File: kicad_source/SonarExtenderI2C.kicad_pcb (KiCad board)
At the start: 2 copper layers, 100 x 60 mm, 48 parts, among them CN2 CONN_01X04, CN3 CONN_01X04, CN4 CONN_01X04, CN5 CONN_01X04, CN6 CONN_01X04, P1 CONN_01X06, U1 NE555-IC_logic, U10 74xx590-IC_logic, U11 74xx590-IC_logic, U12 74xx590-IC_logic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

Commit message: finished pcb layout
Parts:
- removed U19: 74xx32, SOIC:SOIC-14_3.9x8.7mm_Pitch1.27mm
- added C18: C_0603, capacitors:C_0603, F.Cu at (135.4, 56.9)
- added C19: C_0603, capacitors:C_0603, F.Cu at (129.6, 45.0)
- added C2: C_0603, capacitors:C_0603, F.Cu at (142.9, 77.3)
- added C20: C_0603, capacitors:C_0603, F.Cu at (135.1, 44.5)
- added C21: C_0603, capacitors:C_0603, F.Cu at (168.7, 42.2)
- added C22: C_0603, capacitors:C_0603, F.Cu at (153.9, 53.3)
- added L1: Label, labels:jecc_logo_7.2x2.2, F.Cu at (118.0, 45.2)
- added L2: Label, labels:Top, F.Cu at (185.8, 49.6)
- added L3: Label, labels:Bot, F.Cu at (185.6, 49.6)
- added L4: Label, labels:generationmake_logo, F.Cu at (106.0, 61.2)
- added R5: 10k, resistors:R_0603, F.Cu at (180.0, 64.5)
- added R6: 10k, resistors:R_0603, F.Cu at (182.0, 65.5)
- added U3: 74xx08, SOIC:SOIC-14_3.9x8.7mm_Pitch1.27mm, F.Cu at (166.6, 47.8)
- U18: value 74xx08 -> 74xx32
- moved R1 153.5 mm to (96.3, 82.0), turned to 90 degrees
- moved R2 149.6 mm to (101.1, 84.3)
- moved C11 136.0 mm to (113.5, 70.9), turned to 90 degrees
- moved U1 135.7 mm to (101.1, 80.5), turned to 180 degrees
- moved U5 117.0 mm to (127.8, 80.0)
- moved R3 114.1 mm to (101.9, 48.8), turned to 90 degrees
- moved C16 112.2 mm to (104.6, 43.7)
- moved C17 112.1 mm to (108.7, 43.7), turned to 180 degrees
- moved R4 110.6 mm to (106.7, 51.3)
- moved C4 110.5 mm to (98.8, 76.7)
- moved C5 109.9 mm to (103.4, 76.7), turned to 180 degrees
- moved C12 107.2 mm to (127.3, 70.9), turned to 90 degrees
- moved U14 104.7 mm to (106.7, 47.5), turned to 180 degrees
- moved C15 100.2 mm to (111.5, 49.0), turned to 270 degrees
- moved U16 95.7 mm to (127.3, 50.5)
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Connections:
- U1 pad 4: GND -> +3V3
- U13 pad 1: Net-(U13-Pad1) -> /STATUS_ECHO
- U13 pad 10: Net-(U13-Pad10) -> GND
- U13 pad 11: Net-(U13-Pad11) -> GND
- U13 pad 12: Net-(U13-Pad12) -> GND
- U13 pad 13: /STATUS_ECHO -> Net-(U13-Pad13)
- U13 pad 14: Net-(U13-Pad14) -> +3V3
- U13 pad 2: Net-(U13-Pad2) -> /ECHO0
- U13 pad 3: /ECHO0 -> /ECHO1
- U13 pad 4: /ECHO1 -> /ECHO2
- U13 pad 5: /ECHO2 -> /ECHO3
- U13 pad 7: Net-(U13-Pad7) -> GND
- U13 pad 9: Net-(U13-Pad9) -> GND
- U14 pad 4: GND -> +3V3
- U15 pad 5: GND -> /auto/E3
- U15 pad 7: Net-(U15-Pad7) -> I2C_INT
- U16 pad 12: /auto/E3# -> Net-(U15-Pad6)
- U18 pad 1: ENABLE0 -> /auto/E0
- U18 pad 10: ENABLE2 -> /auto/E2
- U18 pad 11: CNT3 -> EN3
- U18 pad 12: /auto/E3# -> T3
- U18 pad 13: ENABLE3 -> /auto/E3
- U18 pad 2: /auto/E0# -> T0
- U18 pad 3: CNT0 -> EN0
- U18 pad 4: ENABLE1 -> /auto/E1
- U18 pad 5: /auto/E1# -> T1
- U18 pad 6: CNT1 -> EN1
- U18 pad 8: CNT2 -> EN2
- U18 pad 9: /auto/E2# -> T2
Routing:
- net +3V3: track 0.00 -> 339.4 mm, vias 0 -> 18
- net /CLK_10KHZ: track 0.00 -> 98.7 mm, vias 0 -> 2
- net +5V: track 0.00 -> 97.5 mm
- net CNT0: track 0.00 -> 97.0 mm, vias 0 -> 2
- net /D7: track 0.00 -> 89.4 mm, vias 0 -> 5
- net /D6: track 0.00 -> 84.9 mm, vias 0 -> 5
- net /D1: track 0.00 -> 83.1 mm, vias 0 -> 5
- net /D2: track 0.00 -> 81.0 mm, vias 0 -> 5
- net AUTO: track 0.00 -> 80.7 mm, vias 0 -> 1
- net /D5: track 0.00 -> 80.5 mm, vias 0 -> 5
- net CNT1: track 0.00 -> 80.4 mm, vias 0 -> 2
- net /D3: track 0.00 -> 79.2 mm, vias 0 -> 5
- net /D4: track 0.00 -> 77.7 mm, vias 0 -> 5
- net /D0: track 0.00 -> 75.1 mm, vias 0 -> 5
- net /TRIG0: track 0.00 -> 71.8 mm, vias 0 -> 2
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- added copper zone on B.Cu, net GND
- added copper zone on F.Cu, net GND

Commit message: reacted to review
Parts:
- added C23: 47uF 16V, capacitors:c_elec_6.3x4.5, F.Cu at (161.9, 67.2)
- added C24: 47uF 16V, capacitors:c_elec_6.3x4.5, F.Cu at (178.7, 93.0)
- added D1: Led_Small, LEDs:LED_0603, F.Cu at (95.2, 74.5)
- added D2: Led_Small, LEDs:LED_0603, F.Cu at (114.4, 92.1)
- added D3: Led_Small, LEDs:LED_0603, F.Cu at (113.6, 73.2)
- added D4: Led_Small, LEDs:LED_0603, F.Cu at (126.6, 73.2)
- added D5: Led_Small, LEDs:LED_0603, F.Cu at (140.6, 73.2)
- added D6: Led_Small, LEDs:LED_0603, F.Cu at (155.0, 73.2)
- added R10: 220, resistors:R_0603, F.Cu at (123.8, 73.2)
- added R11: 220, resistors:R_0603, F.Cu at (137.8, 73.2)
- added R12: 220, resistors:R_0603, F.Cu at (152.2, 73.2)
- added R7: 220, resistors:R_0603, F.Cu at (95.2, 77.3)
- added R8: 320, resistors:R_0603, F.Cu at (113.6, 89.5)
- added R9: 220, resistors:R_0603, F.Cu at (110.8, 73.2)
- C1: value C_0603 -> 1nF
- C10, C11, C12, C13, C14, C18, C19, C2, C20, C21, C22, C3, C5, C6, C7, C8, C9: value C_0603 -> 100nF
- C15: value 100nF -> 1uF
- C16: value 100nF -> 10nF
- C4: value C_0603 -> 10nF
- R1, R3: value R_0603 -> 120k
- R2, R4: value R_0603 -> 12k
- moved L4 2.65 mm to (108.5, 62.2)
- moved L2 0.10 mm to (185.7, 49.6)
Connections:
- U1 pad 1: (no net) -> GND
- U14 pad 1: (no net) -> GND
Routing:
- net GND: track 18.4 -> 49.1 mm, vias 57 -> 62
- net +3V3: track 339.4 -> 347.9 mm, vias 18 -> 19
- net +5V: track 97.5 -> 102.9 mm, vias 0 -> 1
- net CNT0: track 97.0 -> 99.6 mm
- net CNT1: track 80.4 -> 82.4 mm
- net CNT2: track 65.1 -> 67.0 mm
- net CNT3: track 56.3 -> 58.2 mm
- net Net-(D2-Pad2): track 0.00 -> 1.83 mm
- net Net-(D1-Pad2): track 0.00 -> 1.36 mm
- net Net-(D6-Pad2): track 0.00 -> 1.30 mm
- net Net-(D4-Pad2): track 0.00 -> 1.30 mm
- net Net-(D3-Pad2): track 0.00 -> 1.30 mm
- net Net-(D5-Pad2): track 0.00 -> 1.30 mm
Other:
- board text added: "POWER 3V3"
- board text added: "POWER 5V"
- board text added: "SENSOR 0"
- board text added: "SENSOR 1"
- board text added: "SENSOR 2"
- board text added: "SENSOR 3"
- board text added: "SonarExtenderI2C"

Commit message: updated logic table
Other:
- board text added: "v0.1"
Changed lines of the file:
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@@
   (general
     (thickness 1.6)
-    (drawings 15)
+    (drawings 16)
     (tracks 1416)
     (zones 0)
@@
     )
   )
+  (gr_text v0.1 (at 95.1 89.2) (layer F.SilkS)
+    (effects (font (size 1.5 1.5) (thickness 0.3)))
+  )
   (gr_text SonarExtenderI2C (at 93.20784 58.42508 90) (layer F.Cu)

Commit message: added pause mode for automate
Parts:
- D1, D2, D3, D4, D5, D6: value Led_Small -> 150060GS75000
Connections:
- R10 pad 1: CNT1 -> ENABLE1
- R11 pad 1: CNT2 -> ENABLE2
- R12 pad 1: CNT3 -> ENABLE3
- R9 pad 1: CNT0 -> ENABLE0
- U10 pad 14: CNT1 -> ENABLE1
- U10 pad 9: Net-(U10-Pad9) -> (no net)
- U11 pad 14: CNT2 -> ENABLE2
- U11 pad 9: Net-(U11-Pad9) -> (no net)
- U12 pad 14: CNT3 -> ENABLE3
- U12 pad 9: Net-(U12-Pad9) -> (no net)
- U13 pad 13: Net-(U13-Pad13) -> (no net)
- U13 pad 6: Net-(U13-Pad6) -> (no net)
- U13 pad 8: Net-(U13-Pad8) -> (no net)
- U14 pad 3: /auto/CLK_10Hz -> Net-(U14-Pad3)
- U15 pad 10: Net-(U15-Pad10) -> (no net)
- U15 pad 11: Net-(U15-Pad11) -> (no net)
- U15 pad 14: Net-(U15-Pad14) -> (no net)
- U15 pad 15: Net-(U15-Pad15) -> (no net)
- U15 pad 2: Net-(U15-Pad2) -> (no net)
- U15 pad 4: AUTO -> /auto/AUTOEN
- U16 pad 1: AUTO -> /auto/AUTOEN
- U16 pad 2: AUTO -> /auto/AUTOEN
- U17 pad 11: /auto/E2# -> (no net)
- U17 pad 14: /auto/E3# -> (no net)
- U17 pad 3: /auto/E0# -> (no net)
- U17 pad 6: /auto/E1# -> (no net)
- U2 pad 1: Net-(U2-Pad1) -> (no net)
- U3 pad 1: ENABLE0 -> Net-(U14-Pad3)
- U3 pad 10: ENABLE2 -> (no net)
- U3 pad 11: CNT3 -> (no net)
- U3 pad 12: /auto/E3# -> (no net)
- U3 pad 13: ENABLE3 -> (no net)
- U3 pad 2: /auto/E0# -> PAUSE
- U3 pad 3: CNT0 -> /auto/CLK_10Hz
- U3 pad 4: ENABLE1 -> AUTO
- U3 pad 5: /auto/E1# -> PAUSE
- U3 pad 6: CNT1 -> /auto/AUTOEN
- U3 pad 8: CNT2 -> (no net)
- U3 pad 9: /auto/E2# -> (no net)
- U4 pad 10: Net-(U4-Pad10) -> PAUSE
- U4 pad 7: Net-(U4-Pad7) -> (no net)
- U4 pad 9: Net-(U4-Pad9) -> (no net)
- U6 pad 10: Net-(U6-Pad10) -> (no net)
- U6 pad 15: Net-(U6-Pad15) -> (no net)
- U6 pad 2: Net-(U6-Pad2) -> (no net)
- U6 pad 7: Net-(U6-Pad7) -> (no net)
- U7 pad 10: Net-(U7-Pad10) -> (no net)
- U7 pad 12: Net-(U7-Pad12) -> (no net)
- U9 pad 14: CNT0 -> ENABLE0
- U9 pad 9: Net-(U9-Pad9) -> (no net)
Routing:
- net CNT0: track 99.6 -> 0.00 mm, vias 2 -> 0
- net CNT1: track 82.4 -> 0.00 mm, vias 2 -> 0
- net ENABLE0: track 16.6 -> 96.8 mm, vias 2 -> 0
- net ENABLE1: track 11.0 -> 86.0 mm
- net AUTO: track 80.7 -> 11.4 mm, vias 1 -> 0
- net CNT2: track 67.0 -> 0.00 mm, vias 2 -> 0
- net ENABLE2: track 5.45 -> 71.7 mm, vias 0 -> 2
- net /auto/AUTOEN: track 0.00 -> 65.9 mm, vias 0 -> 1
- net Net-(U14-Pad3): track 0.00 -> 58.8 mm
- net CNT3: track 58.2 -> 0.00 mm, vias 2 -> 0
- net ENABLE3: track 5.56 -> 60.0 mm, vias 0 -> 2
- net /auto/E3#: track 35.6 -> 0.00 mm
- net /auto/E2#: track 34.1 -> 0.00 mm, vias 2 -> 0
- net /auto/E0#: track 31.0 -> 0.00 mm
- net /auto/CLK_10Hz: track 61.8 -> 31.3 mm
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
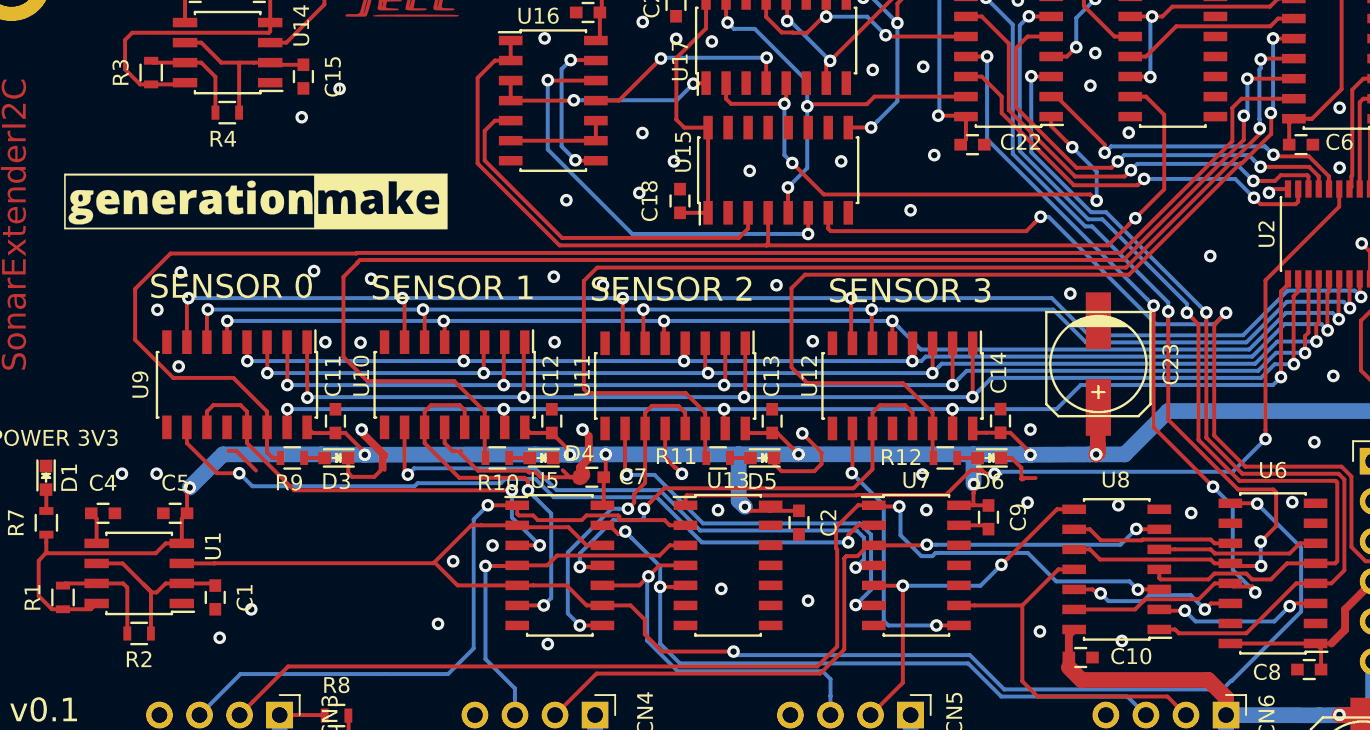
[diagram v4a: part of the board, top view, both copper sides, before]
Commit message: layout changed
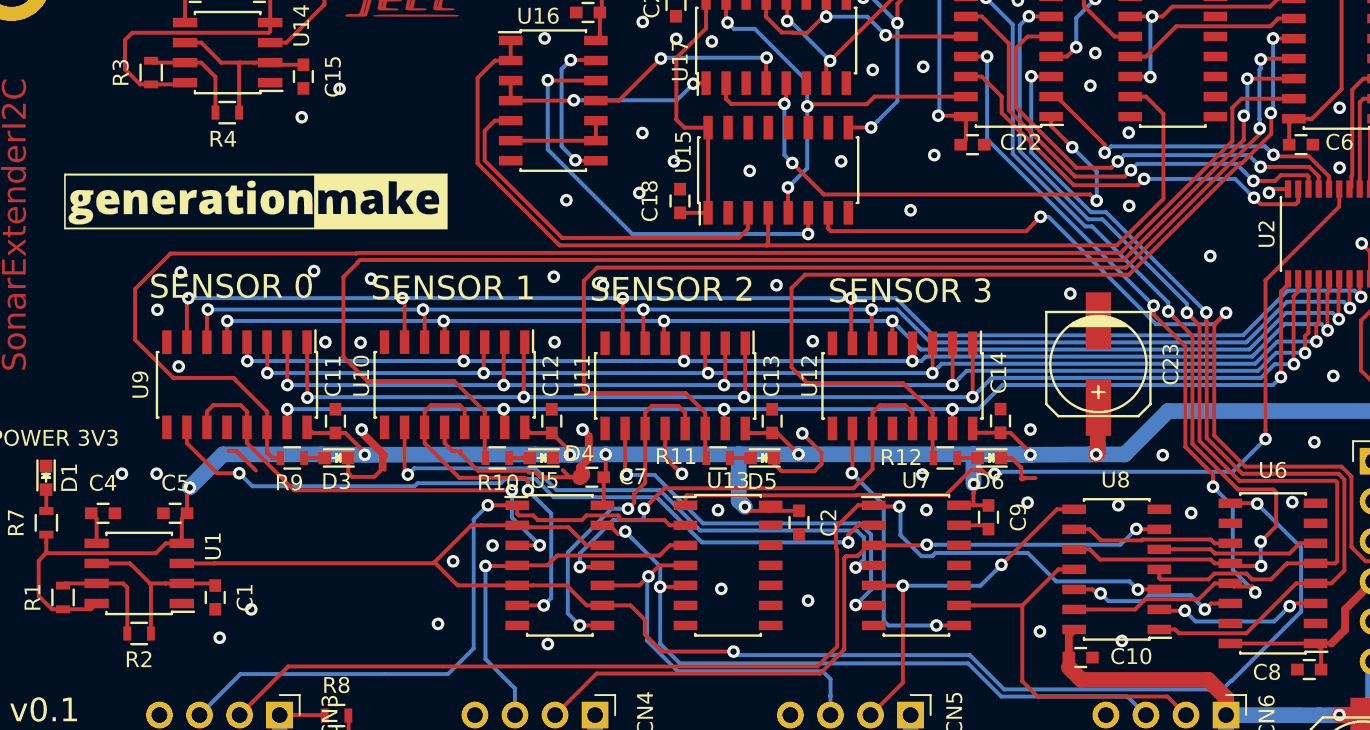
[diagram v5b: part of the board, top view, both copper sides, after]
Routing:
- net Net-(C1-Pad1): track 11.9 -> 11.3 mm
- net /auto/AUTOEN: track 65.9 -> 66.1 mm, vias 1 -> 0
- net GND: vias 68 -> 70

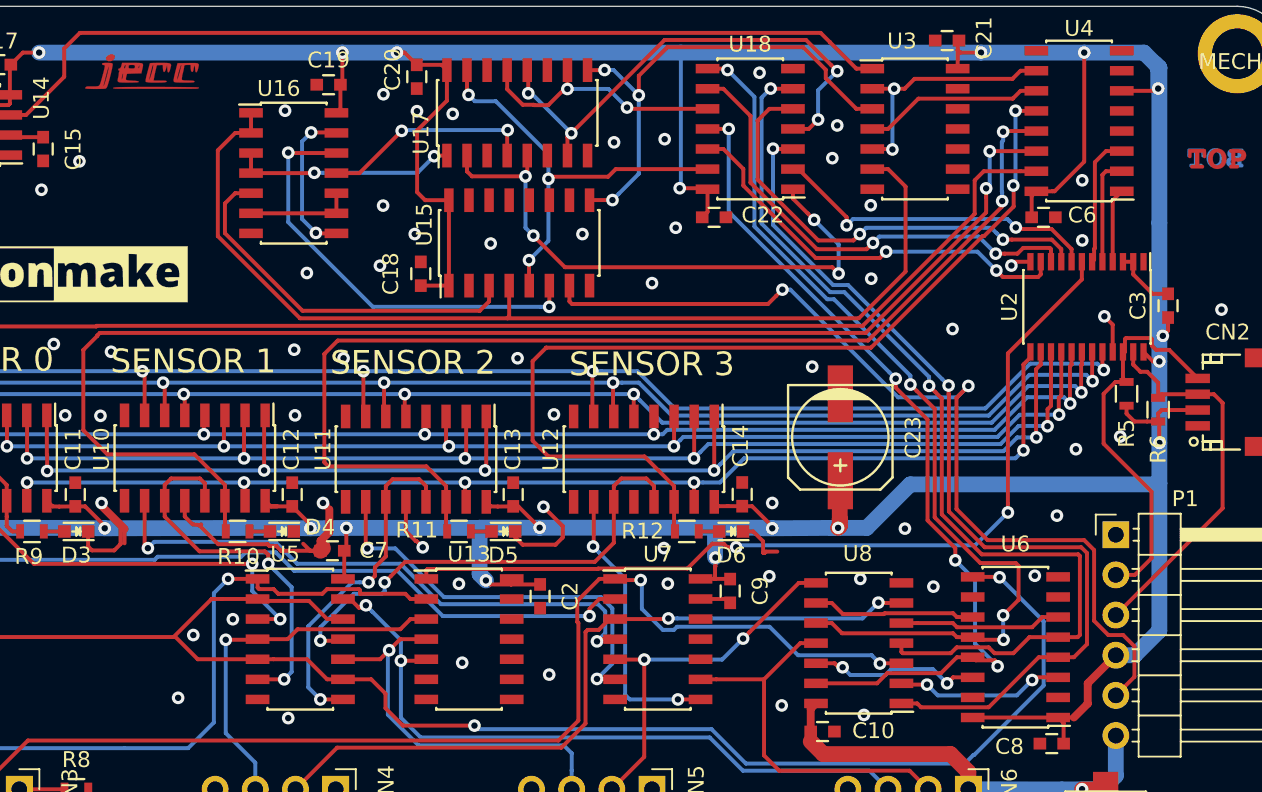
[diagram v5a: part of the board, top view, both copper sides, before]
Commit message: added EN LEDS
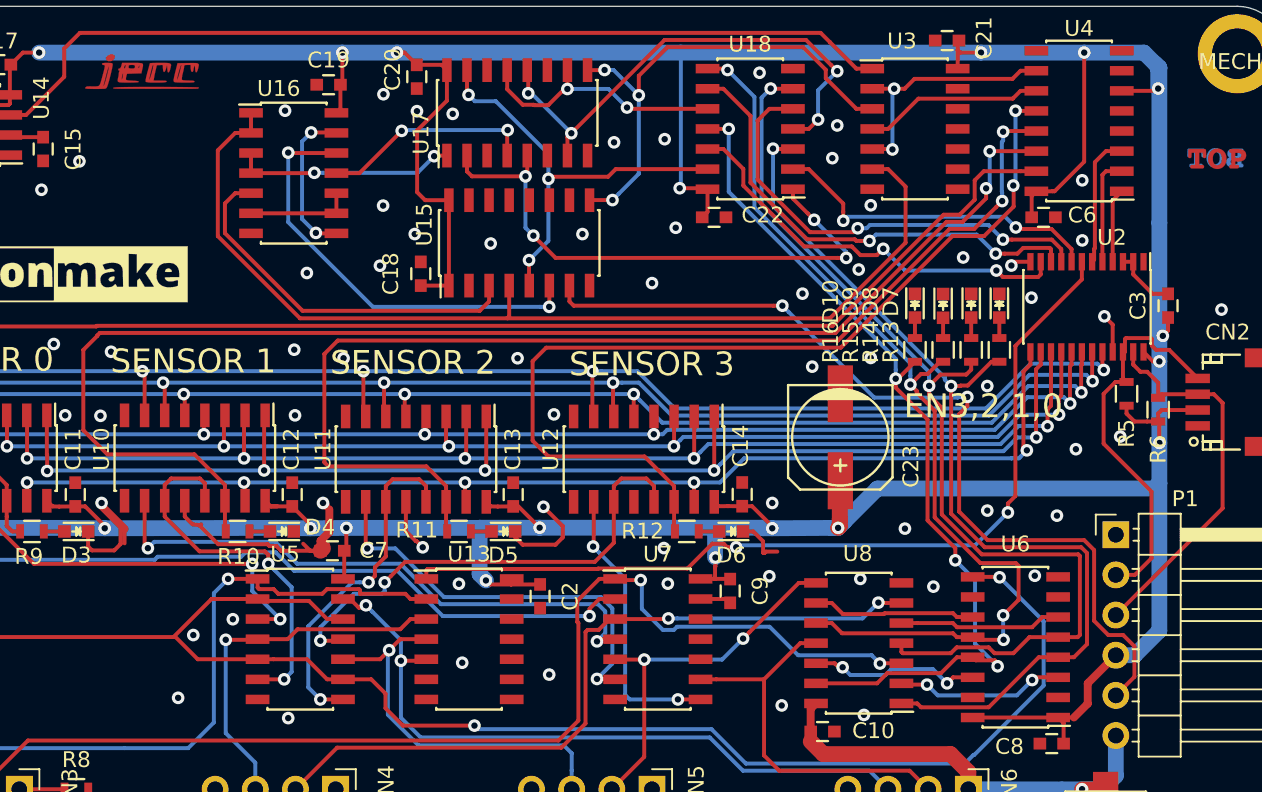
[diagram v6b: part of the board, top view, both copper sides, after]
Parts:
- added D10: 150060GS75000, LEDs:LED_0603, F.Cu at (166.6, 58.9)
- added D7: 150060GS75000, LEDs:LED_0603, F.Cu at (172.0, 58.9)
- added D8: 150060GS75000, LEDs:LED_0603, F.Cu at (170.2, 58.9)
- added D9: 150060GS75000, LEDs:LED_0603, F.Cu at (168.4, 58.9)
- added R13: 220, resistors:R_0603, F.Cu at (172.0, 61.7)
- added R14: 220, resistors:R_0603, F.Cu at (170.2, 61.7)
- added R15: 220, resistors:R_0603, F.Cu at (168.4, 61.7)
- added R16: 220, resistors:R_0603, F.Cu at (166.6, 61.7)
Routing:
- net EN0: track 58.4 -> 61.6 mm
- net EN1: track 61.3 -> 64.4 mm
- net EN2: track 59.2 -> 61.6 mm
- net I2C_INT: track 58.9 -> 57.0 mm
- net EN3: track 54.9 -> 56.5 mm
- net Net-(D8-Pad2): track 0.00 -> 1.29 mm
- net Net-(D7-Pad2): track 0.00 -> 1.29 mm
- net Net-(D10-Pad2): track 0.00 -> 1.29 mm
- net Net-(D9-Pad2): track 0.00 -> 1.28 mm
- net /auto/AUTOEN: track 66.1 -> 65.1 mm
- net /auto/E0: track 36.8 -> 36.1 mm
- net ENABLE0: track 96.8 -> 96.2 mm
- net ENABLE1: track 86.0 -> 85.5 mm
- net GND: vias 70 -> 75
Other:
- board text added: "EN3,2,1,0"
